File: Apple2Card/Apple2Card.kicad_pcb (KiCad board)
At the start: 2 copper layers, 160 x 78.2 mm, 57 parts, among them J1 ICSP, J2 Conn_01x25, J3 Conn_01x25, J4 Conn_01x16, J5 SERCON, J6 WIZNET 5500, SW1 SW_Push, U1 ATmega328P-P, U3 74HCT00, U4 82C55A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

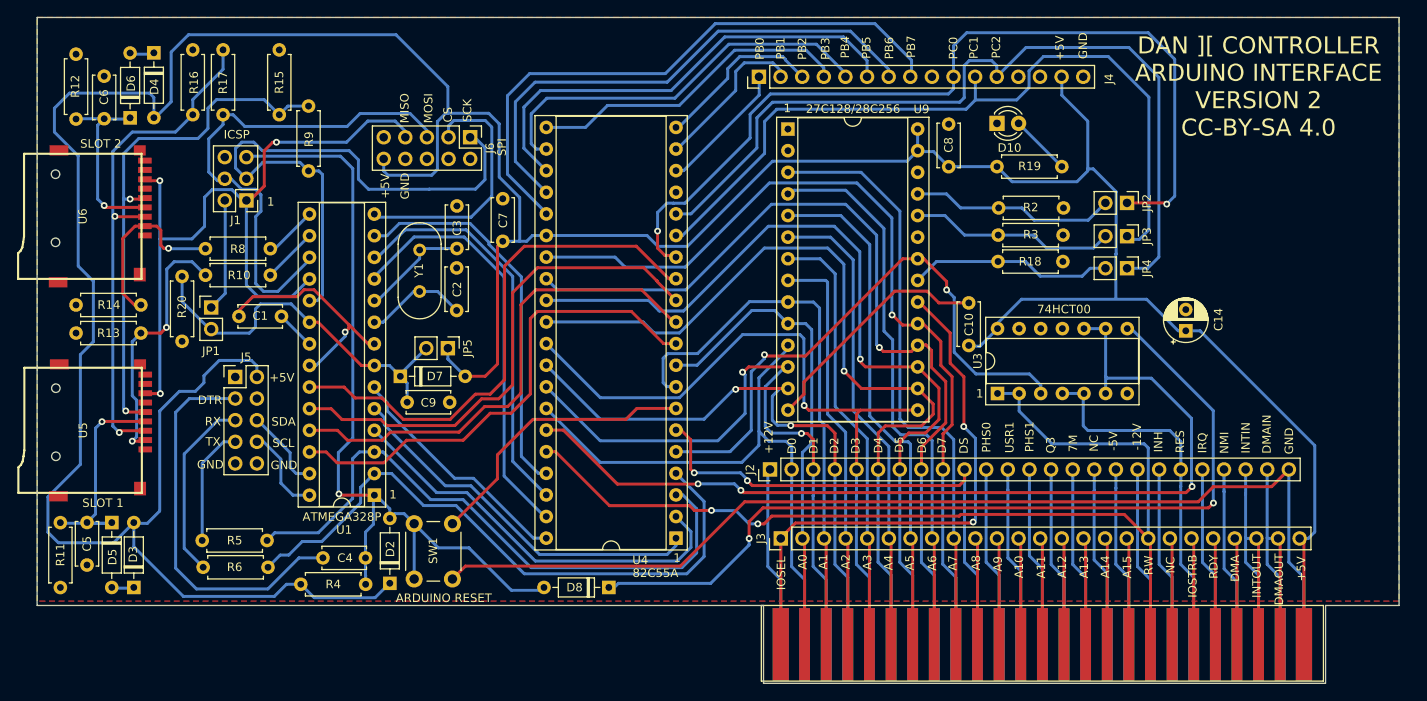
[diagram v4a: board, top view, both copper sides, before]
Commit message: Fixed device select timing bug
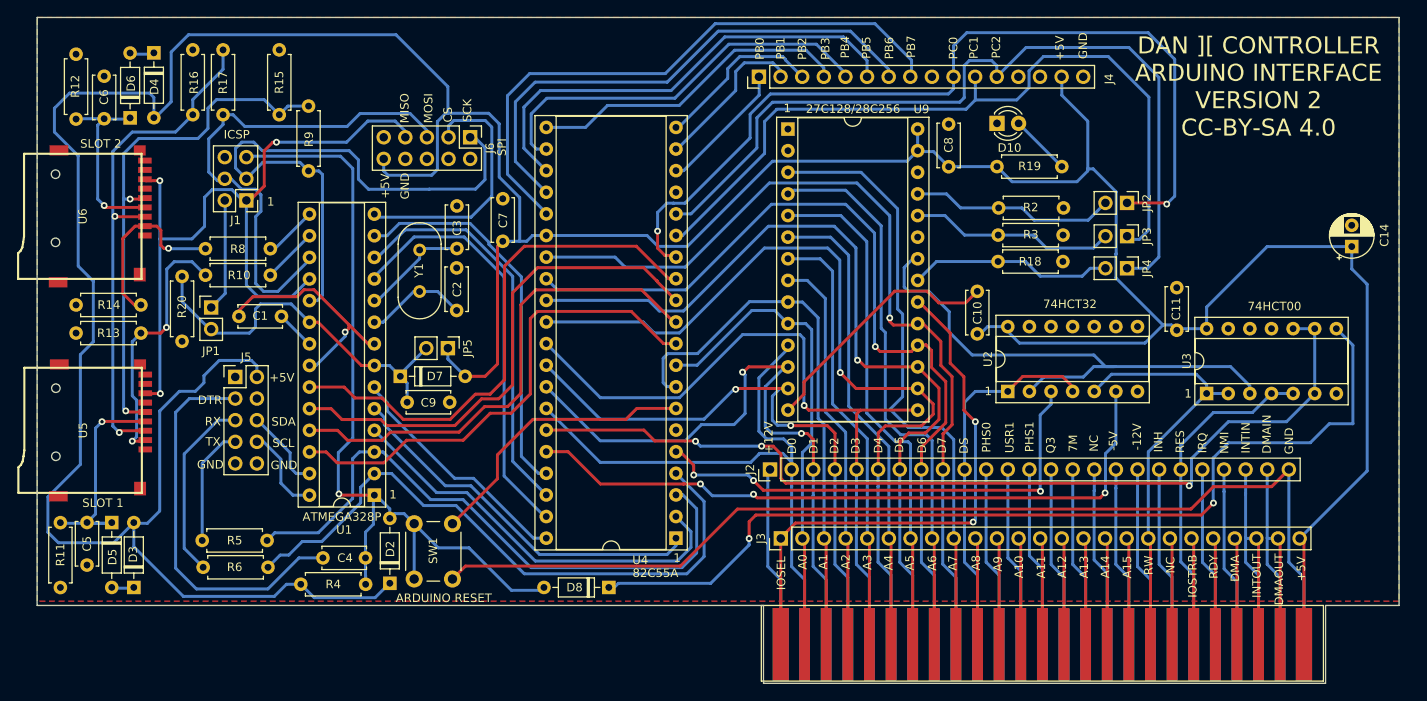
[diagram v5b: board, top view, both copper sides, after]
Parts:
- added C11: 100 nF, Capacitor_THT:C_Disc_D5.0mm_W2.5mm_P5.00mm, F.Cu at (166.9, 62.1)
- added U2: 74HCT32, Package_DIP:DIP-14_W7.62mm_Socket, F.Cu at (147.1, 69.3)
- R18, R2, R3: value 10k -> 4k7
- moved U3 24.6 mm to (170.4, 69.6)
- moved C14 21.9 mm to (187.5, 52.3)
- moved C10 1.69 mm to (143.5, 62.6)
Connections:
- U4 pad 36: RW -> Net-(U4-Pad36)
- U4 pad 5: Net-(U3-Pad3) -> Net-(U4-Pad5)
- U4 pad 6: DS -> GND
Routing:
- net Net-(U4-Pad36): track 0.00 -> 80.8 mm, vias 0 -> 3
- net RW: track 120.6 -> 50.6 mm, vias 2 -> 0
- net Net-(U4-Pad5): track 0.00 -> 57.7 mm, vias 0 -> 3
- net +5V: track 440.4 -> 473.6 mm
- net DS: track 61.4 -> 44.1 mm, vias 2 -> 0
- net Net-(D8-Pad1): track 101.7 -> 112.1 mm
- net RES: track 43.1 -> 39.8 mm
- net D0: track 70.1 -> 73.1 mm
- net Net-(U3-Pad3): track 68.1 -> 65.5 mm, vias 2 -> 0
- net GND: track 214.2 -> 216.4 mm
- net Net-(U3-Pad10): track 109.6 -> 111.3 mm
- net A2: track 48.3 -> 47.0 mm
- net A7: track 71.0 -> 72.2 mm
- net A1: track 65.9 -> 65.1 mm
- net D7: track 102.7 -> 103.3 mm
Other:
- board text added: "74HCT32"

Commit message: Cards and storage works!
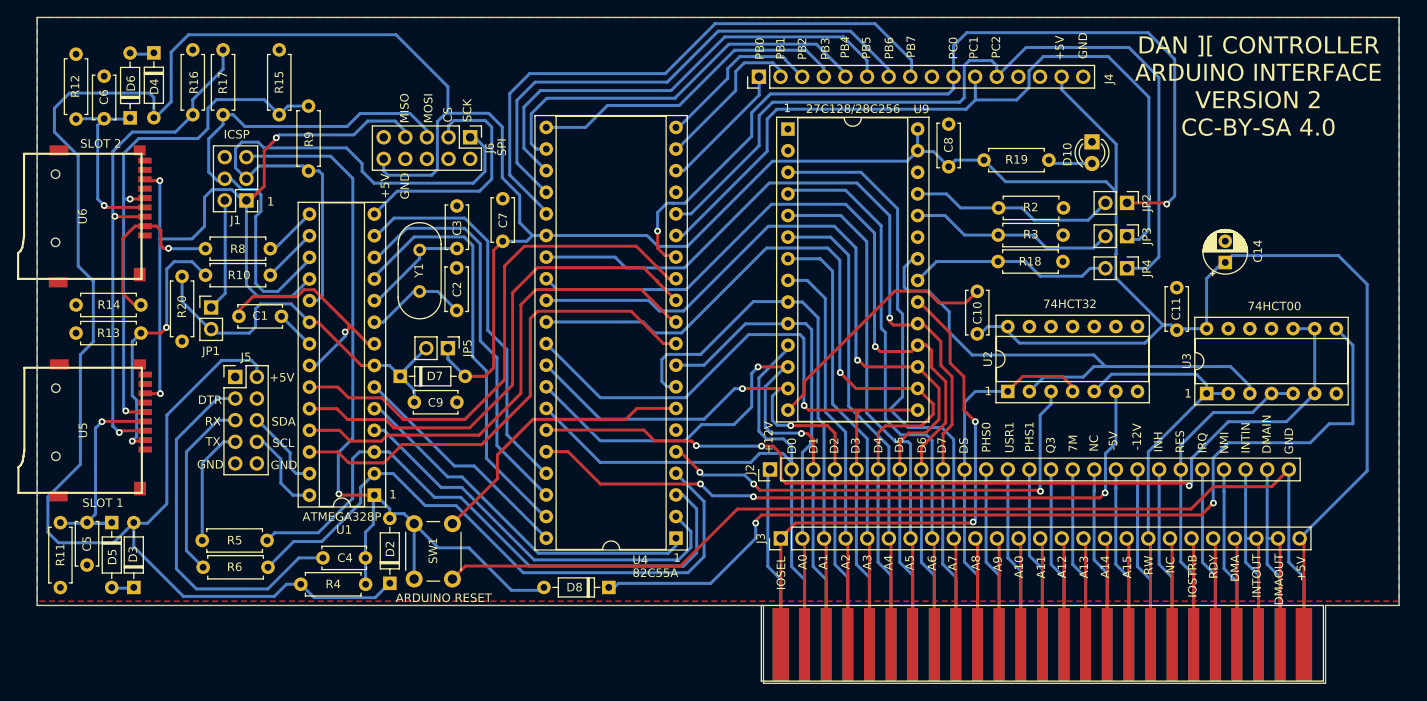
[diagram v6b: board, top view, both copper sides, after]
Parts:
- moved C14 15.0 mm to (172.6, 54.2)
- moved D10 11.4 mm to (157.0, 40.0), turned to -90 degrees
- moved R19 1.70 mm to (144.3, 42.2)
- moved C9 0.85 mm to (77.3, 70.6)
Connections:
- U1 pad 23: OBFA -> STBA
- U1 pad 24: ACKA -> IBFA
- U1 pad 25: STBA -> ACKA
- U1 pad 26: IBFA -> OBFA
- U4 pad 10: IBFA -> OBFA
- U4 pad 11: STBA -> ACKA
- U4 pad 12: ACKA -> IBFA
- U4 pad 13: OBFA -> STBA
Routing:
- net OBFA: track 62.5 -> 57.9 mm
- net STBA: track 58.5 -> 62.5 mm
- net Net-(U2-Pad2): track 65.5 -> 62.2 mm
- net SCK: track 70.1 -> 67.8 mm
- net IBFA: track 57.7 -> 59.8 mm
- net Net-(C4-Pad1): track 45.8 -> 43.8 mm
- net Net-(D10-Pad2): track 7.18 -> 5.23 mm
- net +5V: track 473.6 -> 475.2 mm
- net CS3: track 30.1 -> 28.6 mm
- net A0: track 57.1 -> 55.8 mm
- net D1: track 77.2 -> 76.3 mm
- net ACKA: track 59.5 -> 58.6 mm
- net PD4: track 28.3 -> 27.6 mm
- net RESET: track 99.2 -> 98.5 mm
- net PD3: track 44.4 -> 43.7 mm
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
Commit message: Tweaked edges
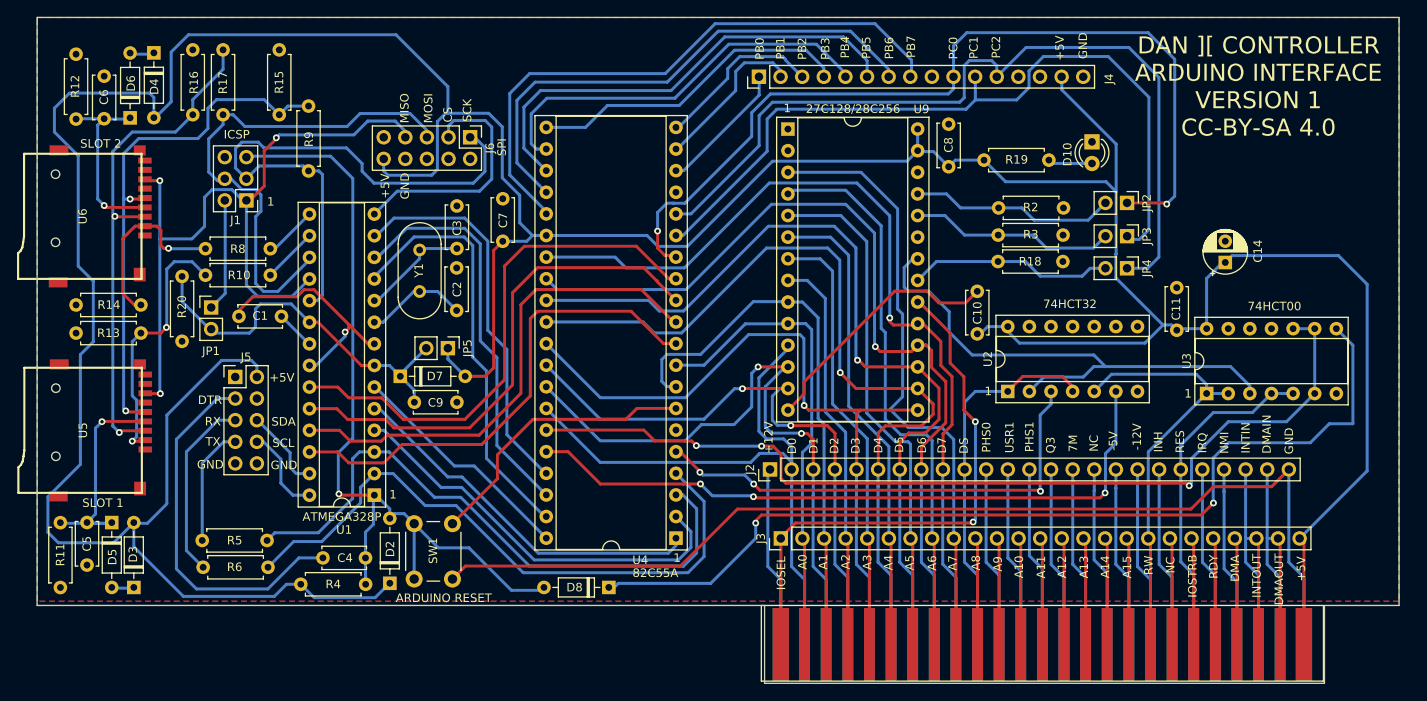
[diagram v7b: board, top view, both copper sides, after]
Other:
- outline, holes or cut-outs redrawn
- board text added: "DAN ][ CONTROLLER ARDUINO INTERFACE VERSION 1 CC-BY-SA 4.0"
- board text removed: "DAN ][ CONTROLLER ARDUINO INTERFACE VERSION 2 CC-BY-SA 4.0"
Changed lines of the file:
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@@
     )
   )
-  (gr_line (start 184.404 94.488) (end 193.04 94.488) (layer "Edge.Cuts") (width 0.1))
-  (gr_line (start 118.364 103.632) (end 184.404 103.632) (layer "Edge.Cuts") (width 0.1))
-  (gr_line (start 33.02 94.488) (end 118.364 94.488) (layer "Edge.Cuts") (width 0.1))
-  (gr_line (start 118.364 94.488) (end 118.364 103.632) (layer "Edge.Cuts") (width 0.1))
+  (gr_line (start 184.277 94.488) (end 193.04 94.488) (layer "Edge.Cuts") (width 0.1))
+  (gr_line (start 118.491 103.632) (end 184.277 103.632) (layer "Edge.Cuts") (width 0.1))
+  (gr_line (start 33.02 94.488) (end 118.491 94.488) (layer "Edge.Cuts") (width 0.1))
+  (gr_line (start 118.491 94.488) (end 118.491 103.632) (layer "Edge.Cuts") (width 0.1))
   (gr_line (start 193.04 25.4) (end 33.02 25.4) (layer "Edge.Cuts") (width 0.1))
   (gr_line (start 33.02 25.4) (end 33.02 94.488) (layer "Edge.Cuts") (width 0.1))
-  (gr_line (start 184.404 103.632) (end 184.404 94.488) (layer "Edge.Cuts") (width 0.1))
+  (gr_line (start 184.277 103.632) (end 184.277 94.488) (layer "Edge.Cuts") (width 0.1))
   (gr_line (start 193.04 94.488) (end 193.04 25.4) (layer "Edge.Cuts") (width 0.1))
   (gr_text "A7" (at 140.6 89.5 90) (layer "F.SilkS")
@@
     (effects (font (size 1 1) (thickness 0.15)))
   )
-  (gr_text "DAN ][ CONTROLLER\nARDUINO INTERFACE\nVERSION 2\nCC-BY-SA 4.0" (at 176.53 33.528) (layer "F.SilkS")
+  (gr_text "DAN ][ CONTROLLER\nARDUINO INTERFACE\nVERSION 1\nCC-BY-SA 4.0" (at 176.53 33.528) (layer "F.SilkS")
     (effects (font (size 2 2) (thickness 0.25)))
   )

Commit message: Added important message
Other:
- board text added: "Apple ][ Forever!"
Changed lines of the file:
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@@
+    (effects (font (size 1 1) (thickness 0.15)))
+  )
+  (gr_text "Apple ][ Forever!" (at 175.895 41.275) (layer "F.SilkS")
     (effects (font (size 1 1) (thickness 0.15)))
   )
